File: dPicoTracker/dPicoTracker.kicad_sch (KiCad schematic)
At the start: 45 parts, among them IC1 ATGM336H-5N31, Q1 AO3401A, Q2 AO3401A, U1 RP2040, U2 NCP1117-3.3_SOT223, U3 CJ431, U4 CJ431, U5 TPS61221DCK, U7 MAX809STRG, U8 BMP280, Y1 Si5351A-B-GT, Y2 XOS25026000LT00351005

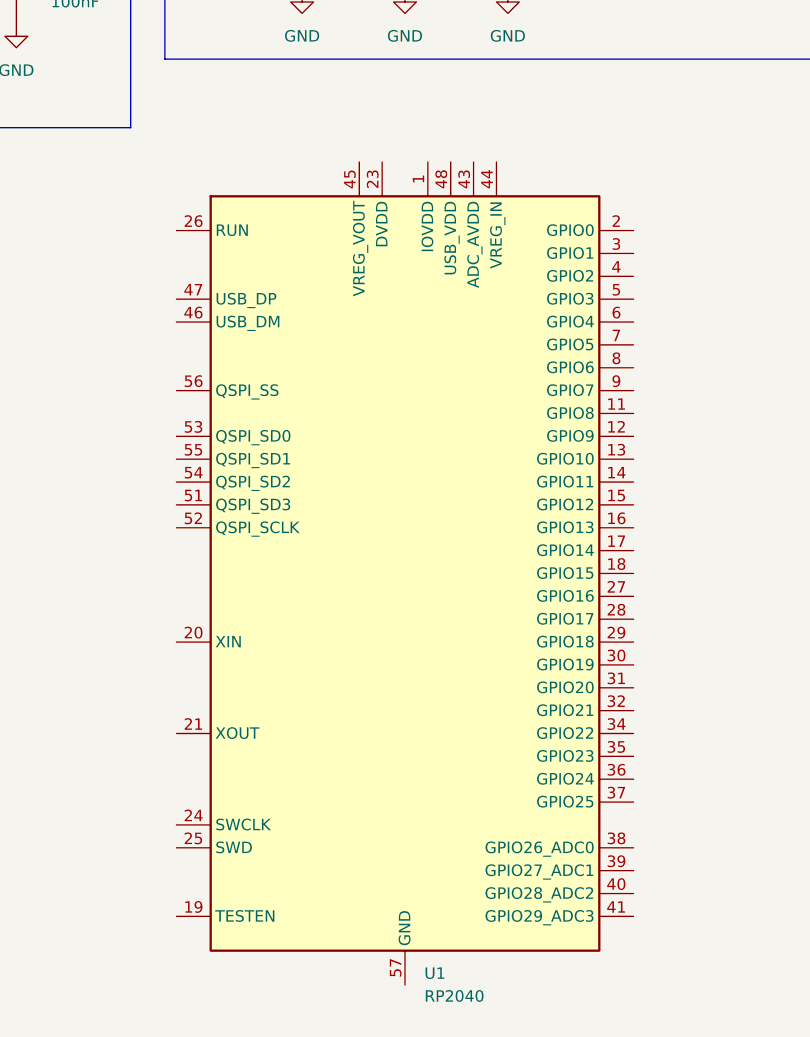
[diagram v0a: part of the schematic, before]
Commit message: swap to pico
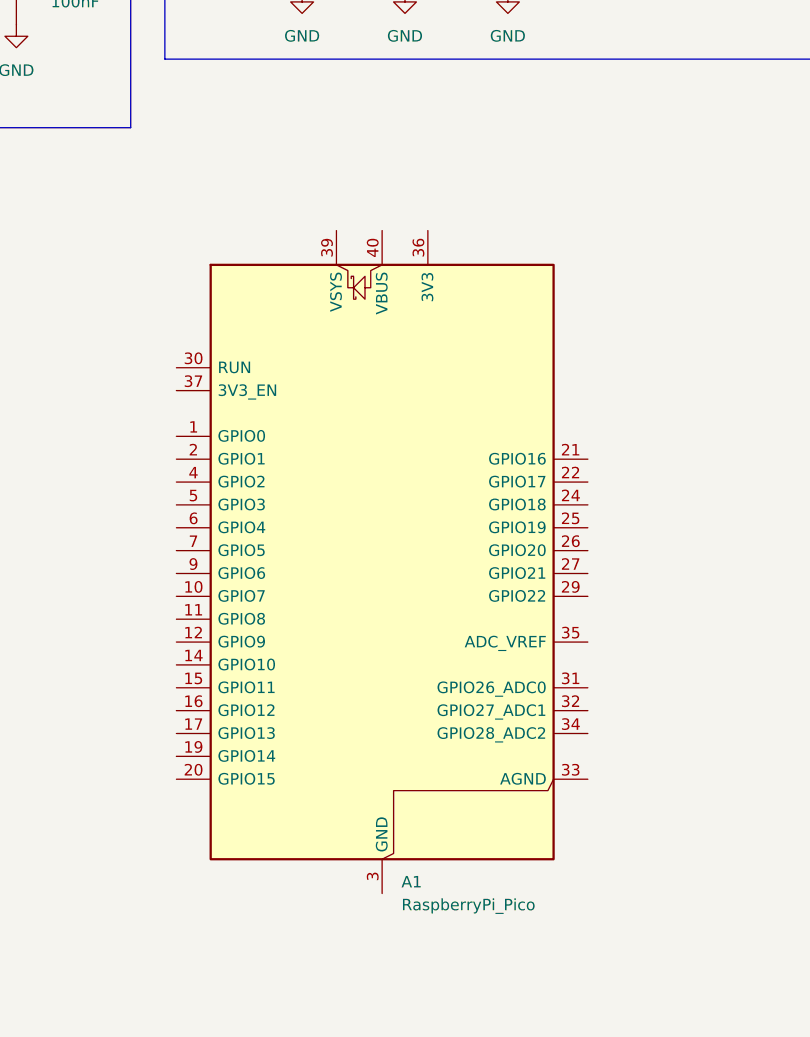
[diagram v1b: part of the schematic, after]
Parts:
- removed U1: RP2040, Package_DFN_QFN:QFN-56-1EP_7x7mm_P0.4mm_EP3.2x3.2mm, symbol MCU_RaspberryPi:RP2040
- added A1: RaspberryPi_Pico, Module:RaspberryPi_Pico_Common_Unspecified, symbol MCU_Module:RaspberryPi_Pico
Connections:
- new net: A1.13 (GND), A1.18 (GND), A1.23 (GND), A1.28 (GND), A1.3 (GND), A1.38 (GND), A1.8 (GND)
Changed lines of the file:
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@@
 	)
 	(symbol
+		(lib_id "MCU_Module:RaspberryPi_Pico")
+		(at 118.11 153.67 0)
+		(unit 1)
+		(exclude_from_sim no)
+		(in_bom yes)
+		(on_board yes)
+		(dnp no)
+		(fields_autoplaced yes)
+		(property "Reference" "A1"
+			(at 120.2533 187.96 0)
+			(effects
+				(font
+					(size 1.27 1.27)
+				)
+				(justify left)
+			)
+		)
+		(property "Value" "RaspberryPi_Pico"
+			(at 120.2533 190.5 0)
+			(effects
+				(font
+					(size 1.27 1.27)
+				)
+				(justify left)
+			)
+		)
+		(property "Footprint" "Module:RaspberryPi_Pico_Common_Unspecified"
+			(at 118.11 200.66 0)
+			(effects
+				(font
+					(size 1.27 1.27)
+				)
+				(hide yes)
+			)
+		)
+		(property "Datasheet" "https://datasheets.raspberrypi.com/pico/pico-datasheet.pdf"
+			(at 118.11 203.2 0)
+			(effects
+				(font
+					(size 1.27 1.27)
+				)
+				(hide yes)
+			)
+		)
+		(property "Description" "Versatile and inexpensive microcontroller module powered by RP2040 dual-core Arm Cortex-M0+ processor up to 133 MHz, 264kB SRAM, 2MB QSPI flash; also supports Raspberry Pi Pico 2"
+			(at 118.11 205.74 0)
+			(effects
+				(font
+					(size 1.27 1.27)
+				)
+				(hide yes)
+			)
+		)
+		(pin "30"
+		)
+		(pin "37"
+		)
+		(pin "1"
+		)
+		(pin "2"
+		)
+		(pin "4"
+		)
+		(pin "5"
+		)
+		(pin "6"
+		)
+		(pin "7"
+		)
+		(pin "9"
+		)
+		(pin "10"
+		)
+		(pin "11"
+		)
+		(pin "18"
+		)
+		(pin "23"
+		)
+		(pin "28"
+		)
+		(pin "3"
+		)
+		(pin "38"
+		)
+		(pin "8"
+		)
+		(pin "36"
+		)
+		(pin "21"
+		)
+		(pin "22"
+		)
+		(pin "24"
+		)
+		(pin "25"
+		)
+		(pin "26"
+		)
+		(pin "27"
+		)
+		(pin "29"
+		)
+		(pin "35"
+		)
+		(pin "31"
+		)
+		(pin "32"
+		)
+		(pin "34"
+		)
+		(pin "33"
+		)
+		(pin "12"
+		)
+		(pin "14"
+		)
+		(pin "15"
+		)
+		(pin "16"
+		)
+		(pin "17"
+		)
+		(pin "19"
+		)
+		(pin "20"
+		)
+		(pin "39"
+		)
+		(pin "40"
+		)
+		(pin "13"
+		)
+		(instances
+			(project ""
+				(path "/762b64d4-eaac-42b3-86d5-cf14f304e7f4"
+					(reference "A1")
+					(unit 1)
+				)
+			)
+		)
+	)
+	(symbol
 		(lib_id "Device:C")
 		(at 207.01 74.93 180)
@@
 					(unit 1)
 				)
-			)
-		)
-	)
-	(symbol
-		(lib_id "MCU_RaspberryPi:RP2040")
-		(at 120.65 153.67 0)
-		(unit 1)
-		(exclude_from_sim no)
-		(in_bom yes)
-		(on_board yes)
-		(dnp no)
-		(fields_autoplaced yes)
-		(property "Reference" "U1"
-			(at 122.7933 198.12 0)
-			(effects
-				(font
-					(size 1.27 1.27)
-				)
-				(justify left)
-			)
-		)
-		(property "Value" "RP2040"
-			(at 122.7933 200.66 0)
-			(effects
-				(font
-					(size 1.27 1.27)
-				)
-				(justify left)
-			)
-		)
-		(property "Footprint" "Package_DFN_QFN:QFN-56-1EP_7x7mm_P0.4mm_EP3.2x3.2mm"
-			(at 120.65 153.67 0)
-			(effects
-				(font
-					(size 1.27 1.27)
-				)
-				(hide yes)
-			)
-		)
-		(property "Datasheet" "https://datasheets.raspberrypi.com/rp2040/rp2040-datasheet.pdf"
-			(at 120.65 153.67 0)
-			(effects
-				(font
-					(size 1.27 1.27)
-				)
-				(hide yes)
-			)
-		)
-		(property "Description" "A microcontroller by Raspberry Pi"
-			(at 120.65 153.67 0)
-			(effects
-				(font
-					(size 1.27 1.27)
-				)
-				(hide yes)
-			)
-		)
-		(pin "26"
-		)
-		(pin "47"
-		)
-		(pin "46"
-		)
-		(pin "56"
-		)
-		(pin "53"
-		)
-		(pin "55"
-		)
-		(pin "54"
-		)
-		(pin "51"
-		)
-		(pin "52"
-		)
-		(pin "20"
-		)
-		(pin "21"
-		)
-		(pin "24"
-		)
-		(pin "25"
-		)
-		(pin "19"
-		)
-		(pin "45"
-		)
-		(pin "23"
-		)
-		(pin "50"
-		)
-		(pin "57"
-		)
-		(pin "1"
-		)
-		(pin "10"
-		)
-		(pin "22"
-		)
-		(pin "33"
-		)
-		(pin "42"
-		)
-		(pin "49"
-		)
-		(pin "48"
-		)
-		(pin "43"
-		)
-		(pin "44"
-		)
-		(pin "2"
-		)
-		(pin "3"
-		)
-		(pin "4"
-		)
-		(pin "5"
-		)
-		(pin "6"
-		)
-		(pin "7"
-		)
-		(pin "8"
-		)
-		(pin "9"
-		)
-		(pin "11"
-		)
-		(pin "12"
-		)
-		(pin "13"
-		)
-		(pin "14"
-		)
-		(pin "15"
-		)
-		(pin "16"
-		)
-		(pin "17"
-		)
-		(pin "18"
-		)
-		(pin "27"
-		)
-		(pin "28"
-		)
-		(pin "29"
-		)
-		(pin "30"
-		)
-		(pin "31"
-		)
-		(pin "32"
-		)
-		(pin "34"
-		)
-		(pin "35"
-		)
-		(pin "36"
-		)
-		(pin "37"
-		)
-		(pin "38"
-		)
-		(pin "39"
-		)
-		(pin "40"
-		)
-		(pin "41"
-		)
-		(instances
-			(project ""
-				(path "/762b64d4-eaac-42b3-86d5-cf14f304e7f4"
-					(reference "U1")
-					(unit 1)
-				)

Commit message: make pcb
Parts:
- removed C3, C4: 10µF, PCM_JLCPCB:C_1206, symbol Device:C
- removed U2: NCP1117-3.3_SOT223, Package_TO_SOT_SMD:SOT-223-3_TabPin2, symbol Regulator_Linear:NCP1117-3.3_SOT223
- AE1, AE2, AE3: footprint (none) -> Connector_PinHeader_2.54mm:PinHeader_1x02_P2.54mm_Vertical
- C10, C11, C12, C13, C14, C15, C16, C17, C18, C19, C9: footprint (none) -> Capacitor_SMD:C_1206_3216Metric
- C5, C7, C8: footprint PCM_JLCPCB:C_1206 -> Capacitor_SMD:C_1206_3216Metric
- IC1: footprint ATGM336H5N31 -> ATGM336H-5N31:ATGM336H5N31
- L1: footprint PCM_JLCPCB:L_1206 -> Inductor_SMD:L_1206_3216Metric
- L2, L3, L4, L5: footprint (none) -> Inductor_SMD:L_1206_3216Metric
- R11, R12, R14, R15, R8, R9: footprint (none) -> Resistor_SMD:R_1206_3216Metric
- R5: footprint PCM_JLCPCB:R_1206 -> Diode_SMD:D_1206_3216Metric
- R6, R7: footprint PCM_JLCPCB:R_1206 -> Capacitor_SMD:C_1206_3216Metric
- U5: footprint Package_TO_SOT_SMD:SOT-23-5 -> Package_TO_SOT_SMD:Texas_R-PDSO-G6
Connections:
- net VBUS is gone; now on net VCC: C5.1, L1.1, R5.1, U5.1 (VIN), U5.6 (EN)
- net +3V3: now also A1.39 (VSYS)
- net GND: now also A1.13 (GND), A1.18 (GND), A1.23 (GND), A1.28 (GND), A1.3 (GND), A1.33 (AGND), A1.38 (GND), A1.8 (GND)
- net GPS_1PPS: now also A1.22 (GPIO17)
- net GPS_ON: now also A1.9 (GPIO6)
- net GPS_PWR_T: now also A1.21 (GPIO16)
- net GPS_RESET: now also A1.7 (GPIO5)
- net MEASURE_VBAT: now also A1.31 (GPIO26_ADC0)
- net RESET: now also A1.30 (RUN)
- net SENS_SCL: now also A1.5 (GPIO3)
- net SENS_SDA: now also A1.4 (GPIO2)
- net UART1_RX: now also A1.12 (GPIO9)
- net UART1_TX: now also A1.11 (GPIO8)
- net VFO_CLK2: now also A1.20 (GPIO15)
- net VFO_PWR_T: now also A1.6 (GPIO4)
- net VFO_SCL: now also A1.17 (GPIO13)
- net VFO_SDA: now also A1.16 (GPIO12)
- net UART0_TX: now reaches A1.1 (GPIO0)
- net UART0_RX: now reaches A1.2 (GPIO1)
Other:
- note removed: "Voltage Regulator"

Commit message: Finish PCB i think
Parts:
- added J1: Conn_01x02_Pin, Connector_PinSocket_2.00mm:PinSocket_1x02_P2.00mm_Vertical, symbol Connector:Conn_01x02_Pin
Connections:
- net GND: now also J1.1 (Pin_1)
- net VCC: now also J1.2 (Pin_2)
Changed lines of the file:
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@@
 	(wire
 		(pts
+			(xy 63.5 33.02) (xy 63.5 27.94)
+		)
+		(stroke
+			(width 0)
+			(type default)
+		)
+	)
+	(wire
+		(pts
 			(xy 55.88 184.15) (xy 55.88 186.69)
 		)
@@
 	(wire
 		(pts
+			(xy 57.15 33.02) (xy 63.5 33.02)
+		)
+		(stroke
+			(width 0)
+			(type default)
+		)
+	)
+	(wire
+		(pts
 			(xy 246.38 46.99) (xy 246.38 38.1)
 		)
@@
 	(wire
 		(pts
+			(xy 63.5 20.32) (xy 63.5 25.4)
+		)
+		(stroke
+			(width 0)
+			(type default)
+		)
+	)
+	(wire
+		(pts
 			(xy 69.85 58.42) (xy 77.47 58.42)
 		)
@@
 		)
 	)
+	(wire
+		(pts
+			(xy 58.42 20.32) (xy 63.5 20.32)
+		)
+		(stroke
+			(width 0)
+			(type default)
+		)
+	)
 	(label "VFO_OSC"
 		(at 229.87 153.67 270)
@@
 	(symbol
 		(lib_id "power:GND")
+		(at 57.15 33.02 0)
+		(unit 1)
+		(exclude_from_sim no)
+		(in_bom yes)
+		(on_board yes)
+		(dnp no)
+		(fields_autoplaced yes)
+		(property "Reference" "#PWR06"
+			(at 57.15 39.37 0)
+			(effects
+				(font
+					(size 1.27 1.27)
+				)
+				(hide yes)
+			)
+		)
+		(property "Value" "GND"
+			(at 57.15 38.1 0)
+			(effects
+				(font
+					(size 1.27 1.27)
+				)
+			)
+		)
+		(property "Footprint" ""
+			(at 57.15 33.02 0)
+			(effects
+				(font
+					(size 1.27 1.27)
+				)
+				(hide yes)
+			)
+		)
+		(property "Datasheet" ""
+			(at 57.15 33.02 0)
+			(effects
+				(font
+					(size 1.27 1.27)
+				)
+				(hide yes)
+			)
+		)
+		(property "Description" "Power symbol creates a global label with name \"GND\" , ground"
+			(at 57.15 33.02 0)
+			(effects
+				(font
+					(size 1.27 1.27)
+				)
+				(hide yes)
+			)
+		)
+		(pin "1"
+		)
+		(instances
+			(project ""
+				(path "/762b64d4-eaac-42b3-86d5-cf14f304e7f4"
+					(reference "#PWR06")
+					(unit 1)
+				)
+			)
+		)
+	)
+	(symbol
+		(lib_id "power:GND")
 		(at 223.52 154.94 0)
 		(unit 1)
@@
 	)
 	(symbol
+		(lib_id "Connector:Conn_01x02_Pin")
+		(at 68.58 27.94 180)
+		(unit 1)
+		(exclude_from_sim no)
+		(in_bom yes)
+		(on_board yes)
+		(dnp no)
+		(fields_autoplaced yes)
+		(property "Reference" "J1"
+			(at 69.85 25.3999 0)
+			(effects
+				(font
+					(size 1.27 1.27)
+				)
+				(justify right)
+			)
+		)
+		(property "Value" "Conn_01x02_Pin"
+			(at 69.85 27.9399 0)
+			(effects
+				(font
+					(size 1.27 1.27)
+				)
+				(justify right)
+			)
+		)
+		(property "Footprint" "Connector_PinSocket_2.00mm:PinSocket_1x02_P2.00mm_Vertical"
+			(at 68.58 27.94 0)
+			(effects
+				(font
+					(size 1.27 1.27)
+				)
+				(hide yes)
+			)
+		)
+		(property "Datasheet" "~"
+			(at 68.58 27.94 0)
+			(effects
+				(font
+					(size 1.27 1.27)
+				)
+				(hide yes)
+			)
+		)
+		(property "Description" "Generic connector, single row, 01x02, script generated"
+			(at 68.58 27.94 0)
+			(effects
+				(font
+					(size 1.27 1.27)
+				)
+				(hide yes)
+			)
+		)
+		(pin "1"
+		)
+		(pin "2"
+		)
+		(instances
+			(project ""
+				(path "/762b64d4-eaac-42b3-86d5-cf14f304e7f4"
+					(reference "J1")
+					(unit 1)
+				)
+			)
+		)
+	)
+	(symbol
 		(lib_id "Device:C")
 		(at 217.17 138.43 0)
@@
 					(unit 1)
 				)
+			)
+		)
+	)
+	(symbol
+		(lib_id "power:VCC")
+		(at 58.42 20.32 0)
+		(unit 1)
+		(exclude_from_sim no)
+		(in_bom yes)
+		(on_board yes)
+		(dnp no)
+		(fields_autoplaced yes)
+		(property "Reference" "#PWR07"
+			(at 58.42 24.13 0)
+			(effects
+				(font
+					(size 1.27 1.27)
+				)
+				(hide yes)
+			)
+		)
+		(property "Value" "VCC"
+			(at 58.42 15.24 0)
+			(effects
+				(font
+					(size 1.27 1.27)
+				)
+			)
+		)
+		(property "Footprint" ""
+			(at 58.42 20.32 0)
+			(effects
+				(font
+					(size 1.27 1.27)
+				)
+				(hide yes)
+			)
+		)
+		(property "Datasheet" ""
+			(at 58.42 20.32 0)
+			(effects
+				(font
+					(size 1.27 1.27)
+				)
+				(hide yes)
+			)
+		)
+		(property "Description" "Power symbol creates a global label with name \"VCC\""
+			(at 58.42 20.32 0)
+			(effects
+				(font
+					(size 1.27 1.27)
+				)
+				(hide yes)
+			)
+		)
+		(pin "1"
+		)
+		(instances
+			(project ""
+				(path "/762b64d4-eaac-42b3-86d5-cf14f304e7f4"
+					(reference "#PWR07")
+					(unit 1)
+				)

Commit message: finishing touches
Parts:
- added C1: 100nF, Capacitor_SMD:C_1206_3216Metric, symbol Device:C
- added J2: Conn_01x05_Pin, Connector_PinSocket_2.54mm:PinSocket_1x05_P2.54mm_Vertical, symbol Connector:Conn_01x05_Pin
- C11, C13: value 240pF -> 180pF
- C12: value 430pF -> 300pF
- C14, C16: value 24pF -> 18pF
- C15: value 43pF -> 30pF
- L2, L3: value 750nH -> 560nH
- L4, L5: value 75nH -> 56nH
- Y2: value XOS25026000LT00351005 -> C132296
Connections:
- net VFO_OSC: now also C1.1; no longer Y1.2 (XA)
- net at A1.24 (GPIO18): now also J2.1 (Pin_1)
- net at A1.25 (GPIO19): now also J2.2 (Pin_2)
- net at A1.26 (GPIO20): now also J2.3 (Pin_3)
- net at A1.27 (GPIO21): now also J2.4 (Pin_4)
- net at A1.29 (GPIO22): now also J2.5 (Pin_5)
- new net: C1.2, Y1.2 (XA)
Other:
- note added: "Crystal, 26MHz P1: GND P2: GND P3: OUT P4: VDD"
- note removed: "Crystal, 26MHz P1: Tri-state P2: GND P3: OUT P4: VDD"
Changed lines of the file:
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@@
 	(rectangle
 		(start 191.77 93.98)
-		(end 266.7 166.37)
+		(end 266.7 170.18)
 		(stroke
 			(width 0)
@@
 		)
 	)
-	(text "Crystal, 26MHz\nP1: Tri-state\nP2: GND\nP3: OUT\nP4: VDD"
+	(text "Crystal, 26MHz\nP1: GND\nP2: GND\nP3: OUT\nP4: VDD"
 		(exclude_from_sim no)
 		(at 197.104 105.156 0)
@@
 	(wire
 		(pts
+			(xy 140.97 153.67) (xy 146.05 153.67)
+		)
+		(stroke
+			(width 0)
+			(type default)
+		)
+	)
+	(wire
+		(pts
 			(xy 83.82 171.45) (xy 95.25 171.45)
 		)
@@
 	(wire
 		(pts
+			(xy 140.97 146.05) (xy 146.05 146.05)
+		)
+		(stroke
+			(width 0)
+			(type default)
+		)
+	)
+	(wire
+		(pts
 			(xy 83.82 148.59) (xy 95.25 148.59)
 		)
@@
 	(wire
 		(pts
+			(xy 229.87 160.02) (xy 229.87 158.75)
+		)
+		(stroke
+			(width 0)
+			(type default)
+		)
+	)
+	(wire
+		(pts
 			(xy 77.47 58.42) (xy 77.47 62.23)
 		)
@@
 	(wire
 		(pts
+			(xy 140.97 156.21) (xy 146.05 156.21)
+		)
+		(stroke
+			(width 0)
+			(type default)
+		)
+	)
+	(wire
+		(pts
 			(xy 120.65 81.28) (xy 118.11 81.28)
 		)
@@
 	(wire
 		(pts
+			(xy 140.97 148.59) (xy 146.05 148.59)
+		)
+		(stroke
+			(width 0)
+			(type default)
+		)
+	)
+	(wire
+		(pts
 			(xy 17.78 123.19) (xy 17.78 125.73)
 		)
@@
 	(wire
 		(pts
+			(xy 140.97 151.13) (xy 146.05 151.13)
+		)
+		(stroke
+			(width 0)
+			(type default)
+		)
+	)
+	(wire
+		(pts
 			(xy 242.57 116.84) (xy 242.57 127)
 		)
@@
 	(wire
 		(pts
-			(xy 229.87 152.4) (xy 229.87 153.67)
-		)
-		(stroke
-			(width 0)
-			(type default)
-		)
-	)
-	(wire
-		(pts
 			(xy 63.5 20.32) (xy 63.5 25.4)
 		)
@@
 	)
 	(label "VFO_OSC"
-		(at 229.87 153.67 270)
+		(at 229.87 158.75 270)
 		(effects
 			(font
@@
 			)
 		)
-		(property "Value" "240pF"
+		(property "Value" "180pF"
 			(at 138.43 62.2299 0)
 			(effects
@@
 			)
 		)
-		(property "Value" "240pF"
+		(property "Value" "180pF"
 			(at 111.76 62.2299 0)
 			(effects
@@
 			)
 		)
-		(property "Value" "75nH"
+		(property "Value" "56nH"
 			(at 114.3 78.74 90)
 			(effects
@@
 			)
 		)
-		(property "Value" "750nH"
+		(property "Value" "560nH"
 			(at 128.27 54.61 90)
 			(effects
@@
 			)
 		)
-		(property "Value" "750nH"
+		(property "Value" "560nH"
 			(at 114.3 54.61 90)
 			(effects
@@
 			)
 		)
-		(property "Value" "24pF"
+		(property "Value" "18pF"
 			(at 135.89 86.3599 0)
 			(effects
@@
 			)
 		)
-		(property "Value" "430pF"
+		(property "Value" "300pF"
 			(at 124.46 62.2299 0)
 			(effects
@@
 	)
 	(symbol
+		(lib_id "Device:C")
+		(at 229.87 156.21 180)
+		(unit 1)
+		(exclude_from_sim no)
+		(in_bom yes)
+		(on_board yes)
+		(dnp no)
+		(fields_autoplaced yes)
+		(property "Reference" "C1"
+			(at 233.68 154.9399 0)
+			(effects
+				(font
+					(size 1.27 1.27)
+				)
+				(justify right)
+			)
+		)
+		(property "Value" "100nF"
+			(at 233.68 157.4799 0)
+			(effects
+				(font
+					(size 1.27 1.27)
+				)
+				(justify right)
+			)
+		)
+		(property "Footprint" "Capacitor_SMD:C_1206_3216Metric"
+			(at 228.9048 152.4 0)
+			(effects
+				(font
+					(size 1.27 1.27)
+				)
+				(hide yes)
+			)
+		)
+		(property "Datasheet" "~"
+			(at 229.87 156.21 0)
+			(effects
+				(font
+					(size 1.27 1.27)
+				)
+				(hide yes)
+			)
+		)
+		(property "Description" "Unpolarized capacitor"
+			(at 229.87 156.21 0)
+			(effects
+				(font
+					(size 1.27 1.27)
+				)
+				(hide yes)
+			)
+		)
+		(pin "2"
+		)
+		(pin "1"
+		)
+		(instances
+			(project ""
+				(path "/762b64d4-eaac-42b3-86d5-cf14f304e7f4"
+					(reference "C1")
+					(unit 1)
+				)
+			)
+		)
+	)
+	(symbol
 		(lib_id "Device:Crystal_GND23")
 		(at 207.01 119.38 90)
@@
 			)
 		)
-		(property "Value" "XOS25026000LT00351005"
+		(property "Value" "C132296"
 			(at 207.01 113.792 90)
 			(effects
@@
 			)
 		)
-		(property "Description" "Four pin crystal, GND on pins 2 and 3"
+		(property "Description" "Four pin crystal, GND on pins 1 and 2"
 			(at 207.01 119.38 0)
 			(effects
@@
 			)
 		)
-		(property "Value" "43pF"
+		(property "Value" "30pF"
 			(at 124.46 86.3599 0)
 			(effects
@@
 			)
 		)
-		(property "Value" "24pF"
+		(property "Value" "18pF"
 			(at 113.03 86.3599 0)
 			(effects
@@
 			)
 		)
-		(property "Value" "75nH"
+		(property "Value" "56nH"
 			(at 128.27 78.74 90)
 			(effects
@@
 					(unit 1)
 				)
+			)
+		)
+	)
+	(symbol
+		(lib_id "Connector:Conn_01x05_Pin")
+		(at 151.13 151.13 0)
+		(mirror y)
+		(unit 1)
+		(exclude_from_sim no)
+		(in_bom yes)
+		(on_board yes)
+		(dnp no)
+		(fields_autoplaced yes)
+		(property "Reference" "J2"
+			(at 152.4 149.8599 0)
+			(effects
+				(font
+					(size 1.27 1.27)
+				)
+				(justify right)
+			)
+		)
+		(property "Value" "Conn_01x05_Pin"
+			(at 152.4 152.3999 0)
+			(effects
+				(font
+					(size 1.27 1.27)
+				)
+				(justify right)
+			)
+		)
+		(property "Footprint" "Connector_PinSocket_2.54mm:PinSocket_1x05_P2.54mm_Vertical"
+			(at 151.13 151.13 0)
+			(effects
+				(font
+					(size 1.27 1.27)
+				)
+				(hide yes)
+			)
+		)
+		(property "Datasheet" "~"
+			(at 151.13 151.13 0)
+			(effects
+				(font
+					(size 1.27 1.27)
+				)
+				(hide yes)
+			)
+		)
+		(property "Description" "Generic connector, single row, 01x05, script generated"
+			(at 151.13 151.13 0)
+			(effects
+				(font
+					(size 1.27 1.27)
+				)
+				(hide yes)
+			)
+		)
+		(pin "4"
+		)
+		(pin "5"
+		)
+		(pin "3"
+		)
+		(pin "1"
+		)
+		(pin "2"
+		)
+		(instances
+			(project ""
+				(path "/762b64d4-eaac-42b3-86d5-cf14f304e7f4"
+					(reference "J2")
+					(unit 1)
+				)

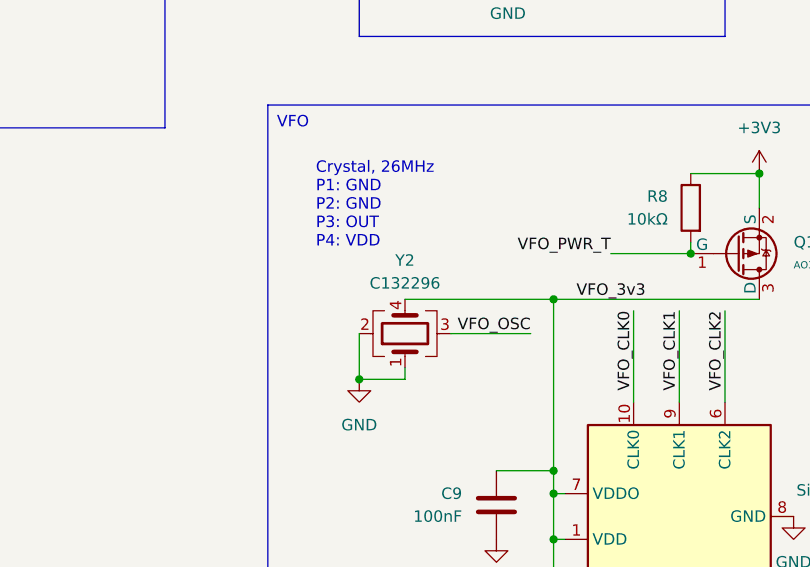
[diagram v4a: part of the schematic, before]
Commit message: fix crystal
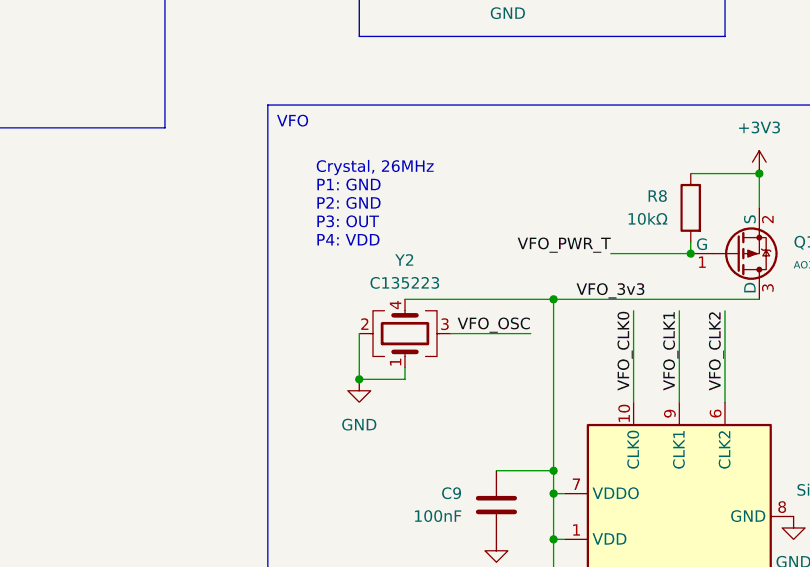
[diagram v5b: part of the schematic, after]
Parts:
- Y2: value C132296 -> C135223
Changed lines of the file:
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@@
 			)
 		)
-		(property "Value" "C132296"
+		(property "Value" "C135223"
 			(at 207.01 113.792 90)
 			(effects
